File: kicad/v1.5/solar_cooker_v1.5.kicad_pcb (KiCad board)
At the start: 2 copper layers, 160.5 x 77.1 mm, 19 parts, among them U1 microSD, U10 GPS, U2 clock_module, U3 anemometer, U4 AM2315, U5 BME680, U6 PT100, U7 pyranometer, U8 PT100, U9 PT100

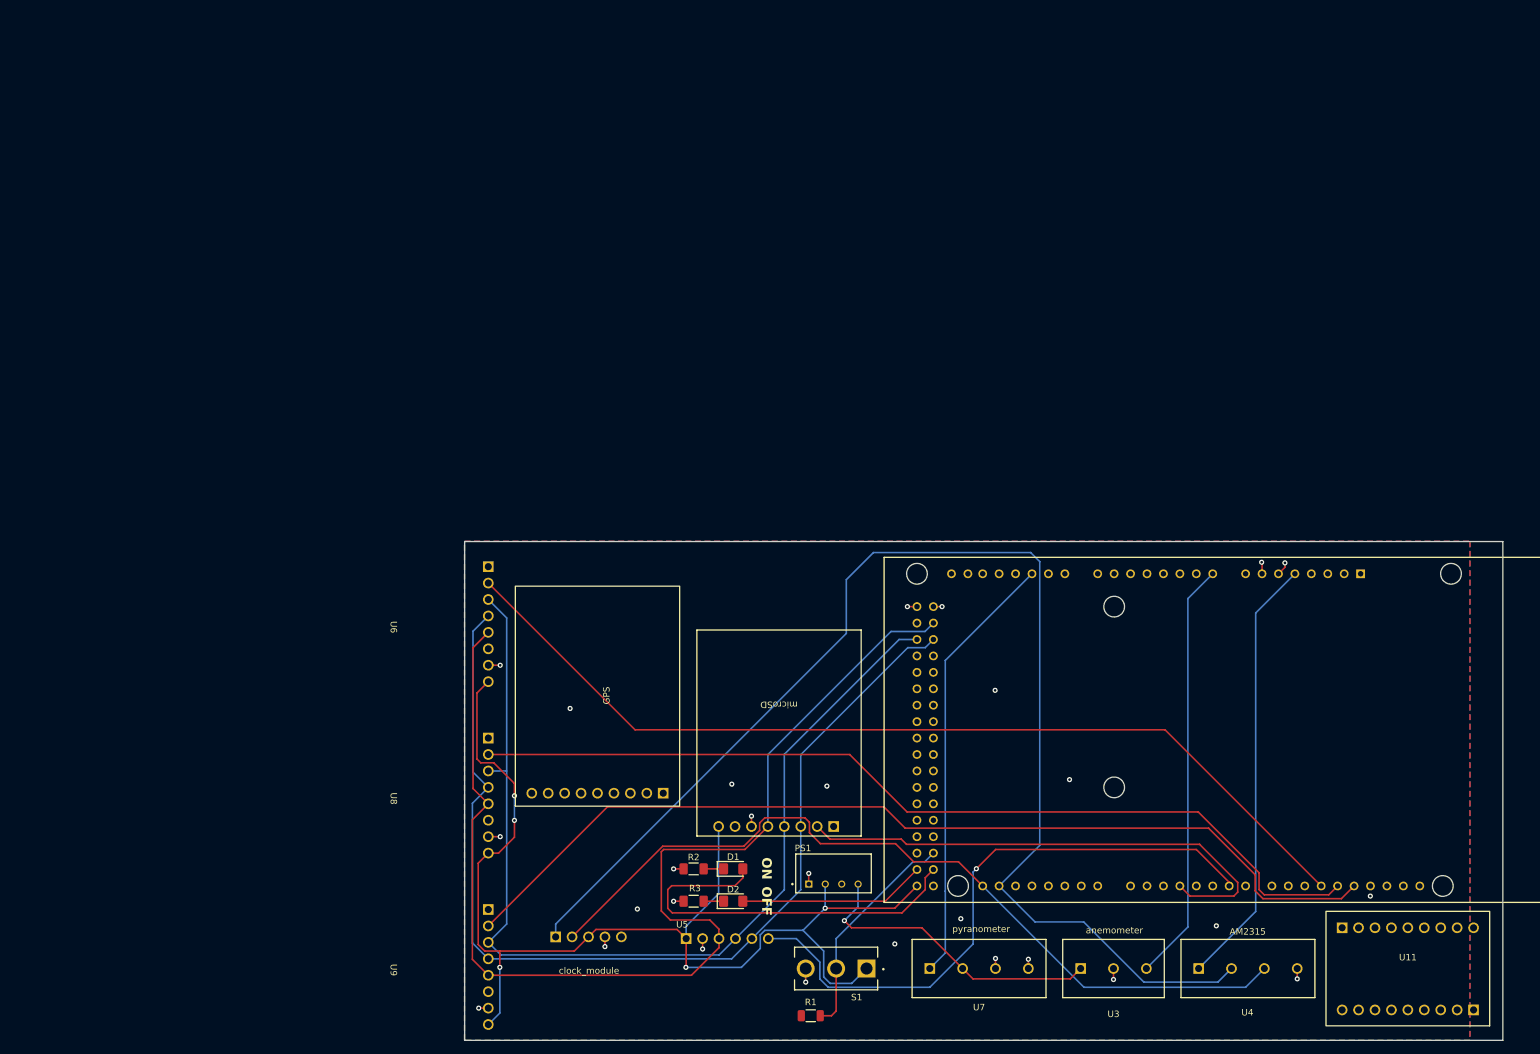
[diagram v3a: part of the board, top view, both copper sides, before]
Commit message: routed display
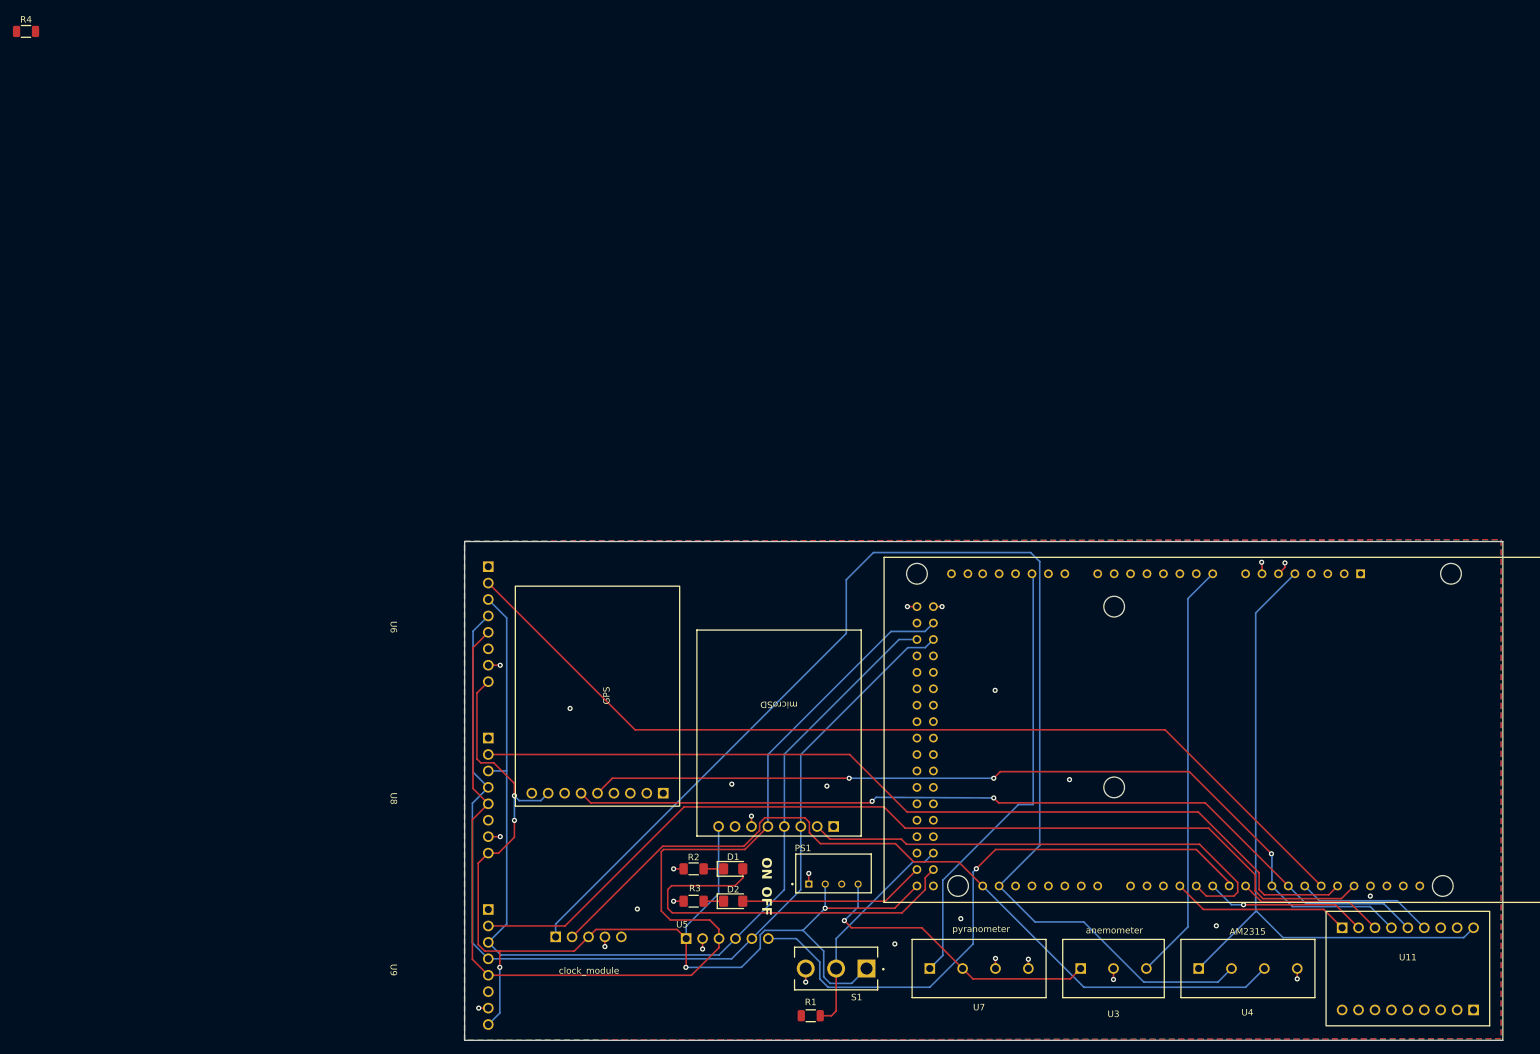
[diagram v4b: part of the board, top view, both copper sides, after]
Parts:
- added R4: 10k, Resistor_SMD:R_1206_3216Metric, F.Cu at (2.31, 1.15)
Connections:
- A1 pad 10: unconnected-(A1-Pad10) -> /D10
- A1 pad 3: /D4 -> /D3
- A1 pad 4: unconnected-(A1-Pad4) -> /D4
- A1 pad 5: unconnected-(A1-Pad5) -> /D5
- A1 pad 7: unconnected-(A1-Pad7) -> /D7
- A1 pad 8: unconnected-(A1-Pad8) -> /D8
- A1 pad 9: unconnected-(A1-Pad9) -> /D9
- U10 pad 2: unconnected-(U10-EN-Pad2) -> Net-(U10-EN)
- U10 pad 4: unconnected-(U10-FIX-Pad4) -> /?
- U10 pad 5: unconnected-(U10-TX-Pad5) -> /D8
- U10 pad 6: unconnected-(U10-RX-Pad6) -> /D9
- U10 pad 7: unconnected-(U10-GND-Pad7) -> GND
- U10 pad 8: unconnected-(U10-VIN-Pad8) -> +5V
- U10 pad 9: unconnected-(U10-PPS-Pad9) -> /?
- U11 pad 1: unconnected-(U11-TCS-Pad1) -> /D3
- U11 pad 2: unconnected-(U11-RST-Pad2) -> /D5
- U11 pad 3: unconnected-(U11-DC-Pad3) -> /D7
- U11 pad 4: unconnected-(U11-MISO-Pad4) -> /D8
- U11 pad 5: unconnected-(U11-MOSI-Pad5) -> /D9
- U11 pad 6: unconnected-(U11-SCK-Pad6) -> /D10
- U11 pad 7: unconnected-(U11-GND-Pad7) -> GND
- U11 pad 9: unconnected-(U11-Vin-Pad9) -> +5V
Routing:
- net /D9: track 0.00 -> 137.4 mm, vias 0 -> 2
- net /D8: track 0.00 -> 137.0 mm, vias 0 -> 3
- net +5V: track 248.3 -> 290.3 mm
- net /D3: track 0.00 -> 27.8 mm
- net /D5: track 0.00 -> 25.2 mm, vias 0 -> 1
- net /D7: track 0.00 -> 22.7 mm
- net /D10: track 0.00 -> 21.2 mm
- net /D4: track 79.9 -> 77.4 mm
- net /A10: track 67.6 -> 69.1 mm

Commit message: rerouted display and gps
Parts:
- moved R4 144.9 mm to (90.9, 115.8), turned to 180 degrees
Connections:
- A1 pad 10: /D10 -> unconnected-(A1-Pad10)
- A1 pad 43: unconnected-(A1-Pad43) -> /D43
- A1 pad 45: unconnected-(A1-Pad45) -> /D45
- A1 pad 8: /D8 -> unconnected-(A1-Pad8)
- A1 pad 9: /D9 -> unconnected-(A1-Pad9)
- U10 pad 4: /? -> unconnected-(U10-FIX-Pad4)
- U10 pad 5: /D8 -> /D43
- U10 pad 6: /D9 -> /D45
- U10 pad 9: /? -> unconnected-(U10-PPS-Pad9)
- U11 pad 4: /D8 -> /MISO
- U11 pad 5: /D9 -> /MOSI
- U11 pad 6: /D10 -> /SCK
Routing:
- net /D9: track 137.4 -> 0.00 mm, vias 2 -> 0
- net /D8: track 137.0 -> 0.00 mm, vias 3 -> 0
- net /SCK: track 179.7 -> 282.6 mm
- net /MISO: track 158.5 -> 257.8 mm
- net /MOSI: track 157.7 -> 253.5 mm
- net /D45: track 0.00 -> 58.6 mm, vias 0 -> 1
- net /D43: track 0.00 -> 55.1 mm, vias 0 -> 1
- net /D10: track 21.2 -> 0.00 mm
- net +5V: track 290.3 -> 298.0 mm
- net Net-(U10-EN): track 0.00 -> 7.14 mm

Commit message: updatet pcb
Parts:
- R2, R3: value 220 -> 150
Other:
- board text added: "Clock"
- board text added: "GPS module"
- board text added: "LCD display"
- board text added: "black"
- board text added: "blue"
- board text added: "brown"
- board text added: "clear"
- board text added: "pt100_1"
- board text added: "pt100_2"
- board text added: "pt100_3"
- board text added: "red"
- board text added: "white"
- board text added: "yellow"
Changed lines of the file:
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@@
         (effects (font (size 1 1) (thickness 0.1)))
     )
-    (fp_text value "BME680" (at -0.14 1.55 unlocked) (layer "F.Fab")
+    (fp_text value "BME680" (at -0.14 1.55 unlocked) (layer "F.SilkS")
         (effects (font (size 1 1) (thickness 0.15)))
     )
@@
     (property "Sheetname" "")
     (attr through_hole)
-    (fp_text reference "U6" (at 0.4 -1.36 -90 unlocked) (layer "F.SilkS")
+    (fp_text reference "U6" (at 0.4 -1.36 -90 unlocked) (layer "Dwgs.User")
         (effects (font (size 1 1) (thickness 0.1)))
     )
@@
     (property "Sheetname" "")
     (attr through_hole)
-    (fp_text reference "U9" (at 0.4 -1.36 -90 unlocked) (layer "F.SilkS")
+    (fp_text reference "U9" (at 0.4 -1.36 -90 unlocked) (layer "Dwgs.User")
         (effects (font (size 1 1) (thickness 0.1)))
     )
@@
     (property "Sheetname" "")
     (attr through_hole)
-    (fp_text reference "U8" (at 0.4 -1.36 -90 unlocked) (layer "F.SilkS")
+    (fp_text reference "U8" (at 0.4 -1.36 -90 unlocked) (layer "Dwgs.User")
         (effects (font (size 1 1) (thickness 0.1)))
     )
@@
     (property "Sheetname" "")
     (attr through_hole)
-    (fp_text reference "U4" (at -0.08 6.8 unlocked) (layer "F.SilkS")
+    (fp_text reference "U4" (at -0.08 6.8 unlocked) (layer "Dwgs.User")
         (effects (font (size 1 1) (thickness 0.1)))
     )
@@
     (property "Sheetname" "")
     (attr through_hole)
-    (fp_text reference "U3" (at 0 7.04 unlocked) (layer "F.SilkS")
+    (fp_text reference "U3" (at 0 7.04 unlocked) (layer "Dwgs.User")
         (effects (font (size 1 1) (thickness 0.1)))
     )
@@
         (effects (font (size 1 1) (thickness 0.1)))
     )
-    (fp_text value "GPS" (at 0.1 1.4 90 unlocked) (layer "F.SilkS")
+    (fp_text value "GPS" (at -3 0.11 180 unlocked) (layer "F.SilkS")
         (effects (font (size 1 1) (thickness 0.15)))
     )
@@
     (property "Sheetname" "")
     (attr through_hole)
-    (fp_text reference "U7" (at 0 6 unlocked) (layer "F.SilkS")
+    (fp_text reference "U7" (at 0 6 unlocked) (layer "Dwgs.User")
         (effects (font (size 1 1) (thickness 0.1)))
     )
@@
     (property "Sheetname" "")
     (attr smd)
-    (fp_text reference "U11" (at 0 -0.5 unlocked) (layer "F.SilkS")
+    (fp_text reference "U11" (at 0 -0.5 unlocked) (layer "Dwgs.User")
         (effects (font (size 1 1) (thickness 0.1)))
     )
@@
         (effects (font (size 1 1) (thickness 0.15)))
     )
-    (fp_text value "220" (at 0 1.82) (layer "F.Fab") hide
+    (fp_text value "150" (at 0 1.82) (layer "F.Fab") hide
         (effects (font (size 1 1) (thickness 0.15)))
     )
@@
         (effects (font (size 1 1) (thickness 0.15)))
     )
-    (fp_text value "220" (at 0 1.82) (layer "F.Fab") hide
+    (fp_text value "150" (at 0 1.82) (layer "F.Fab") hide
         (effects (font (size 1 1) (thickness 0.15)))
     )
@@
     )
   )
+  (gr_line (start 99.95 123.3) (end 77.95 123.3)
+    (stroke (width 0.15) (type default)) (layer "F.SilkS"))
+  (gr_line (start 75.55 80.125) (end 70.1 80.125)
+    (stroke (width 0.15) (type default)) (layer "F.SilkS"))
+  (gr_line (start 75.55 105.525) (end 75.55 80.125)
+    (stroke (width 0.15) (type default)) (layer "F.SilkS"))
+  (gr_line (start 118.9 140.1) (end 118.9 157.1)
+    (stroke (width 0.15) (type default)) (layer "F.SilkS"))
+  (gr_line (start 75.55 132.025) (end 75.55 106.625)
+    (stroke (width 0.15) (type default)) (layer "F.SilkS"))
+  (gr_line (start 75.55 106.625) (end 70.1 106.625)
+    (stroke (width 0.15) (type default)) (layer "F.SilkS"))
+  (gr_line (start 77.95 123.3) (end 77.95 157.1)
+    (stroke (width 0.15) (type default)) (layer "F.SilkS"))
+  (gr_line (start 102.55 140.1) (end 102.55 157.1)
+    (stroke (width 0.15) (type default)) (layer "F.SilkS"))
+  (gr_line (start 70.1 132.025) (end 75.55 132.025)
+    (stroke (width 0.15) (type default)) (layer "F.SilkS"))
+  (gr_line (start 75.55 133.125) (end 75.55 157.1)
+    (stroke (width 0.15) (type default)) (layer "F.SilkS"))
+  (gr_line (start 99.95 157.1) (end 99.95 123.3)
+    (stroke (width 0.15) (type default)) (layer "F.SilkS"))
+  (gr_line (start 70.1 105.525) (end 75.55 105.525)
+    (stroke (width 0.15) (type default)) (layer "F.SilkS"))
+  (gr_line (start 102.55 140.1) (end 118.9 140.1)
+    (stroke (width 0.15) (type default)) (layer "F.SilkS"))
+  (gr_line (start 70.1 133.125) (end 75.55 133.125)
+    (stroke (width 0.15) (type default)) (layer "F.SilkS"))
   (gr_rect (start 70.1 80) (end 230.58 157.1)
     (stroke (width 0.1) (type default)) (fill none) (layer "Edge.Cuts"))
@@
   (gr_rect (start 21.5 16.4) (end 171.5 76.4)
     (stroke (width 0.2) (type default)) (fill none) (layer "User.1"))
+  (gr_text "black" (at 152.125 148.75) (layer "F.SilkS")
+    (effects (font (size 1 1) (thickness 0.15)))
+  )
   (gr_text "ON" (at 115.9 128.8 -90) (layer "F.SilkS")
     (effects (font (size 1.5 1.5) (thickness 0.3) bold) (justify left bottom))
   )
+  (gr_text "white" (at 142.2 148.75) (layer "F.SilkS")
+    (effects (font (size 1 1) (thickness 0.15)))
+  )
+  (gr_text "red" (at 147.1 148.75) (layer "F.SilkS")
+    (effects (font (size 1 1) (thickness 0.15)))
+  )
+  (gr_text "SD card" (at 112.5 99.9) (layer "F.SilkS")
+    (effects (font (size 2 2) (thickness 0.3)) (justify left bottom))
+  )
+  (gr_text "white" (at 193.825 148.75) (layer "F.SilkS")
+    (effects (font (size 1 1) (thickness 0.15)))
+  )
+  (gr_text "blue" (at 175.525 148.75) (layer "F.SilkS")
+    (effects (font (size 1 1) (thickness 0.15)))
+  )
+  (gr_text "yellow" (at 188.65 148.75) (layer "F.SilkS")
+    (effects (font (size 1 1) (thickness 0.15)))
+  )
+  (gr_text "brown" (at 165.35 148.75) (layer "F.SilkS")
+    (effects (font (size 1 1) (thickness 0.15)))
+  )
+  (gr_text "blue" (at 198.725 148.75) (layer "F.SilkS")
+    (effects (font (size 1 1) (thickness 0.15)))
+  )
+  (gr_text "Clock" (at 84.75 130.75) (layer "F.SilkS")
+    (effects (font (size 2 2) (thickness 0.3)) (justify left bottom))
+  )
+  (gr_text "red" (at 183.55 148.75) (layer "F.SilkS")
+    (effects (font (size 1 1) (thickness 0.15)))
+  )
+  (gr_text "LCD display" (at 207.325 149.2) (layer "F.SilkS")
+    (effects (font (size 2 2) (thickness 0.3)) (justify left bottom))
+  )
   (gr_text "OFF" (at 115.9 133.3 -90) (layer "F.SilkS")
     (effects (font (size 1.5 1.5) (thickness 0.3) bold) (justify left bottom))
   )
+  (gr_text "pt100_2" (at 71.75 119.1 -90) (layer "F.SilkS")
+    (effects (font (size 1 1) (thickness 0.15)))
+  )
+  (gr_text "pt100_1" (at 71.675 92.175 -90) (layer "F.SilkS")
+    (effects (font (size 1 1) (thickness 0.15)))
+  )
+  (gr_text "pt100_3" (at 71.675 144.975 -90) (layer "F.SilkS")
+    (effects (font (size 1 1) (thickness 0.15)))
+  )
+  (gr_text "black" (at 170.5 148.75) (layer "F.SilkS")
+    (effects (font (size 1 1) (thickness 0.15)))
+  )
+  (gr_text "GPS module" (at 81.325 94.575) (layer "F.SilkS")
+    (effects (font (size 2 2) (thickness 0.3)) (justify left bottom))
+  )
+  (gr_text "clear" (at 157.275 148.75) (layer "F.SilkS")
+    (effects (font (size 1 1) (thickness 0.15)))
+  )
   (gr_text "top side of the box" (at 276.3 75.7 270) (layer "User.1")
     (effects (font (size 2 2) (thickness 0.3)) (justify left bottom))
   )
-  (gr_text "SD card" (at 112.5 99.9) (layer "User.1")
-    (effects (font (size 2 2) (thickness 0.3)) (justify left bottom))
-  )
